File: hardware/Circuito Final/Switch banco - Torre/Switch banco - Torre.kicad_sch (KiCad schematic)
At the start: 60 parts, among them J1 Conn_01x07, J2 Conn_02x07_Odd_Even, J3 Conn_01x07, Q1 MMBFJ112, Q1_1 MMBT2222A, Q3 MMBT2222A, U1 74HC595, U2 74HC4051

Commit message: comienza arreglo de huellas
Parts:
- added R2_11, R2_12: 0, Resistor_SMD:R_1206_3216Metric_Pad1.30x1.75mm_HandSolder, symbol Device:R
- U1: footprint Package_DIP:DIP-16_W7.62mm_SMDSocket_SmallPads -> Package_SO:SOIC-16_3.9x9.9mm_P1.27mm
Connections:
- net DATA: now also J2.14 (Pin_14); no longer J2.11 (Pin_11)
- net clock: now also J2.13 (Pin_13), R2_11.1, R2_11.2; no longer J2.14 (Pin_14)
- net latch: now also J2.12 (Pin_12), R2_12.1, R2_12.2; no longer J2.13 (Pin_13)
- net reset: now also J2.11 (Pin_11); no longer J2.12 (Pin_12)
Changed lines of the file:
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@@
 		)
 	)
+	(label "DATA"
+		(at 161.29 147.32 0)
+		(effects
+			(font
+				(size 1.27 1.27)
+			)
+			(justify left bottom)
+		)
+	)
 	(label "cell_neg5"
 		(at 39.37 165.1 0)
@@
 		)
 	)
+	(label "latch"
+		(at 163.83 66.04 270)
+		(effects
+			(font
+				(size 1.27 1.27)
+			)
+			(justify right bottom)
+		)
+	)
 	(label "Vcell3"
 		(at 73.66 163.83 180)
@@
 		)
 	)
+	(label "clock"
+		(at 146.05 55.88 90)
+		(effects
+			(font
+				(size 1.27 1.27)
+			)
+			(justify left bottom)
+		)
+	)
 	(label "reset"
 		(at 27.94 102.87 180)
@@
 		)
 	)
-	(label "reset"
-		(at 161.29 144.78 0)
-		(effects
-			(font
-				(size 1.27 1.27)
-			)
-			(justify left bottom)
-		)
-	)
-	(label "DATA"
-		(at 148.59 144.78 180)
-		(effects
-			(font
-				(size 1.27 1.27)
-			)
-			(justify right bottom)
-		)
-	)
 	(label "Vcell4"
 		(at 92.71 73.66 0)
@@
 		)
 	)
+	(label "clock"
+		(at 146.05 63.5 270)
+		(effects
+			(font
+				(size 1.27 1.27)
+			)
+			(justify right bottom)
+		)
+	)
+	(label "latch"
+		(at 161.29 144.78 0)
+		(effects
+			(font
+				(size 1.27 1.27)
+			)
+			(justify left bottom)
+		)
+	)
 	(label "Bit_1"
 		(at 30.48 34.29 180)
@@
 		)
 	)
+	(label "reset"
+		(at 148.59 144.78 180)
+		(effects
+			(font
+				(size 1.27 1.27)
+			)
+			(justify right bottom)
+		)
+	)
 	(label "Vcell6"
 		(at 73.66 171.45 180)
@@
 		)
 	)
-	(label "latch"
+	(label "clock"
 		(at 148.59 147.32 180)
 		(effects
@@
 		)
 	)
-	(label "clock"
-		(at 161.29 147.32 0)
-		(effects
-			(font
-				(size 1.27 1.27)
-			)
-			(justify left bottom)
-		)
-	)
 	(label "Vcc"
 		(at 148.59 142.24 180)
@@
 		)
 	)
+	(label "latch"
+		(at 163.83 58.42 90)
+		(effects
+			(font
+				(size 1.27 1.27)
+			)
+			(justify left bottom)
+		)
+	)
 	(label "bus_pos"
 		(at 148.59 137.16 180)
@@
 	(symbol
 		(lib_id "Device:R")
+		(at 146.05 59.69 0)
+		(unit 1)
+		(body_style 1)
+		(exclude_from_sim no)
+		(in_bom yes)
+		(on_board yes)
+		(in_pos_files yes)
+		(dnp no)
+		(property "Reference" "R2_11"
+			(at 148.59 58.4199 0)
+			(show_name no)
+			(do_not_autoplace no)
+			(effects
+				(font
+					(size 1.27 1.27)
+				)
+				(justify left)
+			)
+		)
+		(property "Value" "0"
+			(at 147.574 60.96 0)
+			(show_name no)
+			(do_not_autoplace no)
+			(effects
+				(font
+					(size 1.27 1.27)
+				)
+				(justify left)
+			)
+		)
+		(property "Footprint" "Resistor_SMD:R_1206_3216Metric_Pad1.30x1.75mm_HandSolder"
+			(at 144.272 59.69 90)
+			(hide yes)
+			(show_name no)
+			(do_not_autoplace no)
+			(effects
+				(font
+					(size 1.27 1.27)
+				)
+			)
+		)
+		(property "Datasheet" ""
+			(at 146.05 59.69 0)
+			(hide yes)
+			(show_name no)
+			(do_not_autoplace no)
+			(effects
+				(font
+					(size 1.27 1.27)
+				)
+			)
+		)
+		(property "Description" "Resistor"
+			(at 146.05 59.69 0)
+			(hide yes)
+			(show_name no)
+			(do_not_autoplace no)
+			(effects
+				(font
+					(size 1.27 1.27)
+				)
+			)
+		)
+		(pin "1"
+		)
+		(pin "2"
+		)
+		(instances
+			(project "Switch banco - Torre"
+				(path "/0f6cbaa3-1a93-4070-b53f-b642439dda2a"
+					(reference "R2_11")
+					(unit 1)
+				)
+			)
+		)
+	)
+	(symbol
+		(lib_id "Device:R")
 		(at 48.26 52.07 0)
 		(unit 1)
@@
 	)
 	(symbol
+		(lib_id "Device:R")
+		(at 163.83 62.23 0)
+		(unit 1)
+		(body_style 1)
+		(exclude_from_sim no)
+		(in_bom yes)
+		(on_board yes)
+		(in_pos_files yes)
+		(dnp no)
+		(property "Reference" "R2_12"
+			(at 166.37 60.9599 0)
+			(show_name no)
+			(do_not_autoplace no)
+			(effects
+				(font
+					(size 1.27 1.27)
+				)
+				(justify left)
+			)
+		)
+		(property "Value" "0"
+			(at 165.354 63.5 0)
+			(show_name no)
+			(do_not_autoplace no)
+			(effects
+				(font
+					(size 1.27 1.27)
+				)
+				(justify left)
+			)
+		)
+		(property "Footprint" "Resistor_SMD:R_1206_3216Metric_Pad1.30x1.75mm_HandSolder"
+			(at 162.052 62.23 90)
+			(hide yes)
+			(show_name no)
+			(do_not_autoplace no)
+			(effects
+				(font
+					(size 1.27 1.27)
+				)
+			)
+		)
+		(property "Datasheet" ""
+			(at 163.83 62.23 0)
+			(hide yes)
+			(show_name no)
+			(do_not_autoplace no)
+			(effects
+				(font
+					(size 1.27 1.27)
+				)
+			)
+		)
+		(property "Description" "Resistor"
+			(at 163.83 62.23 0)
+			(hide yes)
+			(show_name no)
+			(do_not_autoplace no)
+			(effects
+				(font
+					(size 1.27 1.27)
+				)
+			)
+		)
+		(pin "1"
+		)
+		(pin "2"
+		)
+		(instances
+			(project "Switch banco - Torre"
+				(path "/0f6cbaa3-1a93-4070-b53f-b642439dda2a"
+					(reference "R2_12")
+					(unit 1)
+				)
+			)
+		)
+	)
+	(symbol
 		(lib_id "74xx:74HC595")
 		(at 38.1 105.41 0)
@@
 			)
 		)
-		(property "Footprint" "Package_DIP:DIP-16_W7.62mm_SMDSocket_SmallPads"
+		(property "Footprint" "Package_SO:SOIC-16_3.9x9.9mm_P1.27mm"
 			(at 38.1 105.41 0)
 			(hide yes)

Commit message: pruebas del shift register
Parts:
- removed Rp9: 10k, Resistor_SMD:R_1206_3216Metric_Pad1.30x1.75mm_HandSolder, symbol Device:R
- removed Rs0: 330, Resistor_SMD:R_1206_3216Metric_Pad1.30x1.75mm_HandSolder, symbol Device:R
- added C1, C2: 100n, Capacitor_SMD:C_1206_3216Metric_Pad1.33x1.80mm_HandSolder, symbol Device:C
- added Rs8: 330, Resistor_SMD:R_1206_3216Metric_Pad1.30x1.75mm_HandSolder, symbol Device:R
- U2: footprint Package_DIP:DIP-16_W7.62mm_SMDSocket_SmallPads -> Package_SO:SOIC-16_3.9x9.9mm_P1.27mm
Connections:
- net GND: now also C1.2, C2.2
- net Vbanco: now also Rs8.1
- net Vcc: now also J2.13 (Pin_13), U1.10 (~{SRCLR}), C1.1, C2.1; no longer J2.9 (Pin_9)
- net cell_neg5: now also R1_2.2; no longer R1_1.2
- net cell_neg6: now also R1_1.2; no longer R1_2.2
- net clock: no longer J2.13 (Pin_13), R2_11.1
- net latch: no longer J2.12 (Pin_12), R2_12.2
- net reset: now also J2.12 (Pin_12); no longer J2.11 (Pin_11), U1.10 (~{SRCLR})
- net at Rp1.1, U1.15 (QA): now also Rs8.2
- new net: J2.9 (Pin_9), R2_11.1
- new net: J2.11 (Pin_11), R2_12.2
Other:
- moved on the sheet: R2_11, R2_12

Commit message: Sube version 2.1 del banco
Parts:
- added R2_13, R2_14: 0, Resistor_SMD:R_1206_3216Metric_Pad1.30x1.75mm_HandSolder, symbol Device:R
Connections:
- net reset is gone; now on net latch: J2.12 (Pin_12)
- net GND: now also J2.9 (Pin_9), R2_12.1, R2_12.2, R2_13.1, R2_13.2, R2_14.1, R2_14.2
- net Vcc: now also R2_11.1, R2_11.2
- net clock: now also J2.11 (Pin_11); no longer R2_11.2
- net latch: no longer R2_12.1
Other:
- moved on the sheet: R2_10, R2_8, R2_9

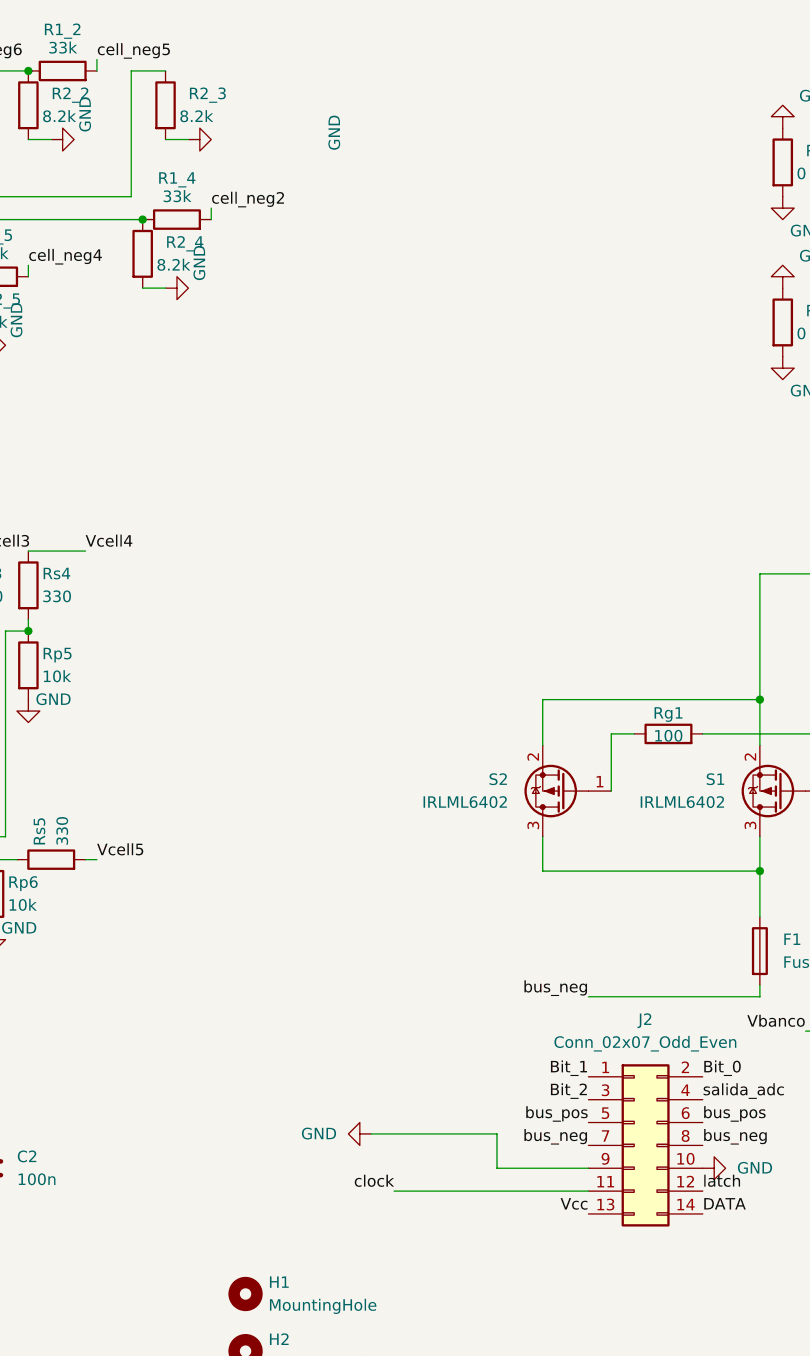
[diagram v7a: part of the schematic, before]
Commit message: agrego test points en el banco
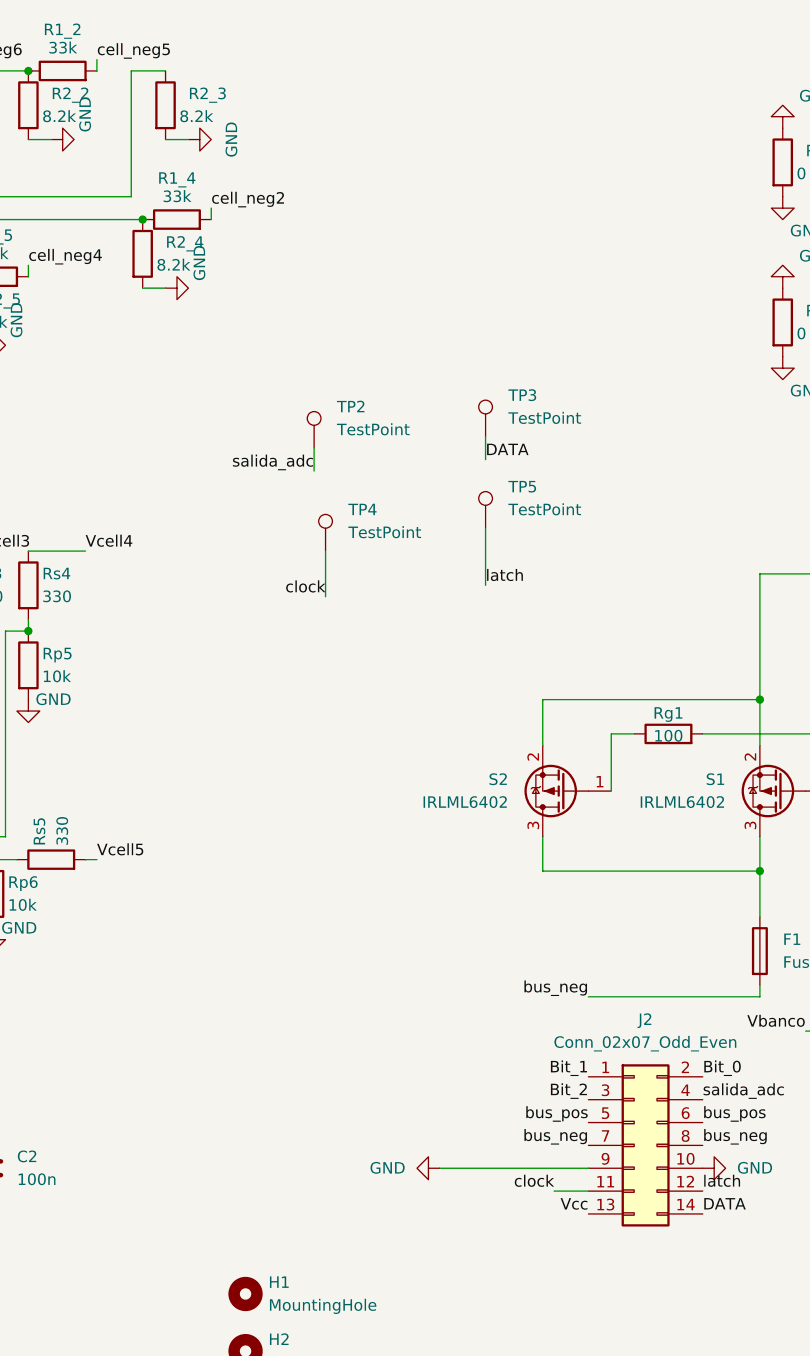
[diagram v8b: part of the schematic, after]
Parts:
- added TP2, TP3, TP4, TP5: TestPoint, TestPoint:TestPoint_Loop_D2.54mm_Drill1.5mm_Beaded, symbol Connector:TestPoint
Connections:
- net DATA: now also TP3.1
- net clock: now also TP4.1
- net latch: now also TP5.1
- net salida_adc: now also TP2.1
